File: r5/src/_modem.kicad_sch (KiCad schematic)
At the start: 59 parts, among them J1 , J12 U_FL-R-SMT-1_10_, J13 JAE_SIM_Card_SF72S006, J17 DNP, J2 , J3 , J4 , J5 , J6 , J7 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

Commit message: Rename Manufacturer field
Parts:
- U7: MANUFACTURER Sierra Wireliess -> (none); Manufacturer (none) -> Sierra Wireliess
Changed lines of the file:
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@@
       (effects (font (size 1.27 1.27)) hide)
     )
-    (property "MANUFACTURER" "Sierra Wireliess" (at 139.7 143.51 0)
+    (property "Manufacturer" "Sierra Wireliess" (at 139.7 143.51 0)
       (effects (font (size 1.27 1.27)) (justify left bottom) hide)
     )

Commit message: Change 0805 47uF to 1206 to save a BOM line. Update layout, DRC pass.
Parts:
- C22, C23: footprint Capacitor_SMD:C_0805_2012Metric -> Capacitor_SMD:C_1206_3216Metric
- C26: MPN (none) -> GRM155R71H104KE14D; Manufacturer (none) -> Murata; Mouser (none) -> 81-GRM155R71H104KE4D; Voltage (none) -> 50V

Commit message: Oops, hadn't run the ERC for ages. Ran, passed. Add ERC and DRC exclusions where unavoidable
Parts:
- C21: Tempco (none) -> NP0
- C22, C23: MPN (none) -> GRM31CE70J476ME15L; Manufacturer (none) -> Murata; Mouser (none) -> 81-GRM31CE70J476ME5L
- D3: Digikey (none) -> 475-2488-6-ND; MPN (none) -> LOR976-PS-1; Manufacturer (none) -> Osram; Mouser (none) -> 720-LOR976-PS-1
- D6, D9: Digikey (none) -> 283-2964-6-ND; MPN (none) -> 0402ESDA-MLP1; Manufacturer (none) -> Eaton; Mouser (none) -> 504-0402ESDA-MLP1
- J12: Digikey (none) -> J983DKR-ND; MPN (none) -> 128-0711-201; Manufacturer (none) -> Cinch Johnson; Mouser (none) -> 530-1280711201
- J13: Digikey (none) -> 670-2967-6-ND; MPN (none) -> SF72S006VBDR2500; Manufacturer (none) -> JAE; Mouser (none) -> 656-SF72S006VBDR2500
- Q11, Q5, Q6, Q7, Q8, Q9: Digikey (none) -> 1727-1280-6-ND; MPN (none) -> NX3008NBKW; Manufacturer (none) -> Nexperia; Mouser (none) -> 771-NX3008NBKW,115
- U7: MPN (none) -> RC7620; Manufacturer Sierra Wireliess -> Sierra Wireless
- U8: Digikey (none) -> ESD7004MUTAGOSDKR-ND; MPN (none) -> ESD7004MUTAG; Manufacturer (none) -> On Semi; Mouser (none) -> 863-ESD7004MUTAG

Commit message: Exclude all testpoints from BoM. Correct some BoM errors
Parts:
- T1, T10, T11, T8, T9: now left out of the parts list

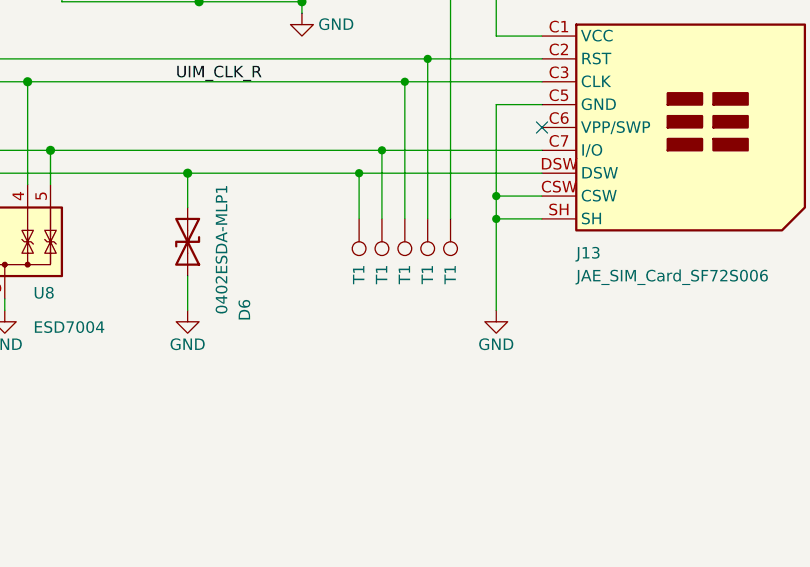
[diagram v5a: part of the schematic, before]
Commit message: Update to new Kicad nightly - file format update
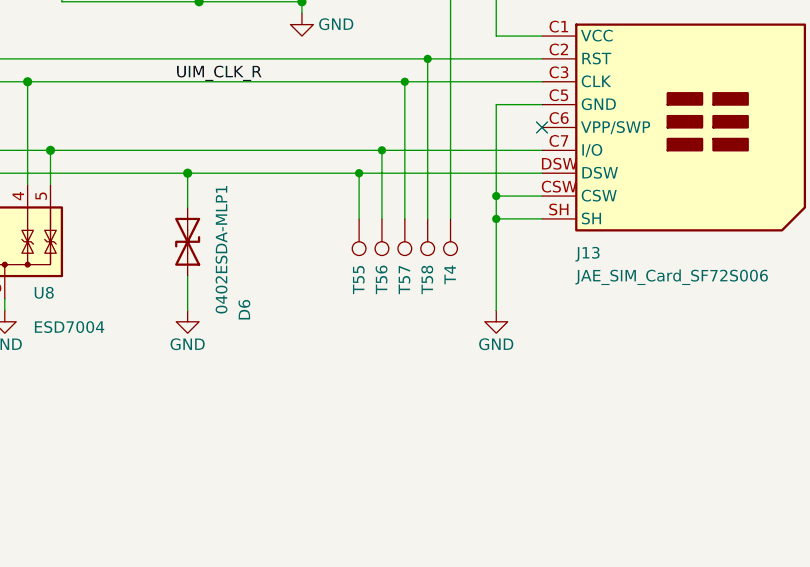
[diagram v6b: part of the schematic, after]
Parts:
- renumbered T1 to T4, T1 to T55, T1 to T56, T1 to T57, T1 to T58
